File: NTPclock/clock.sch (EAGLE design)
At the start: 28 parts, among them IC1 MAX7219CNG

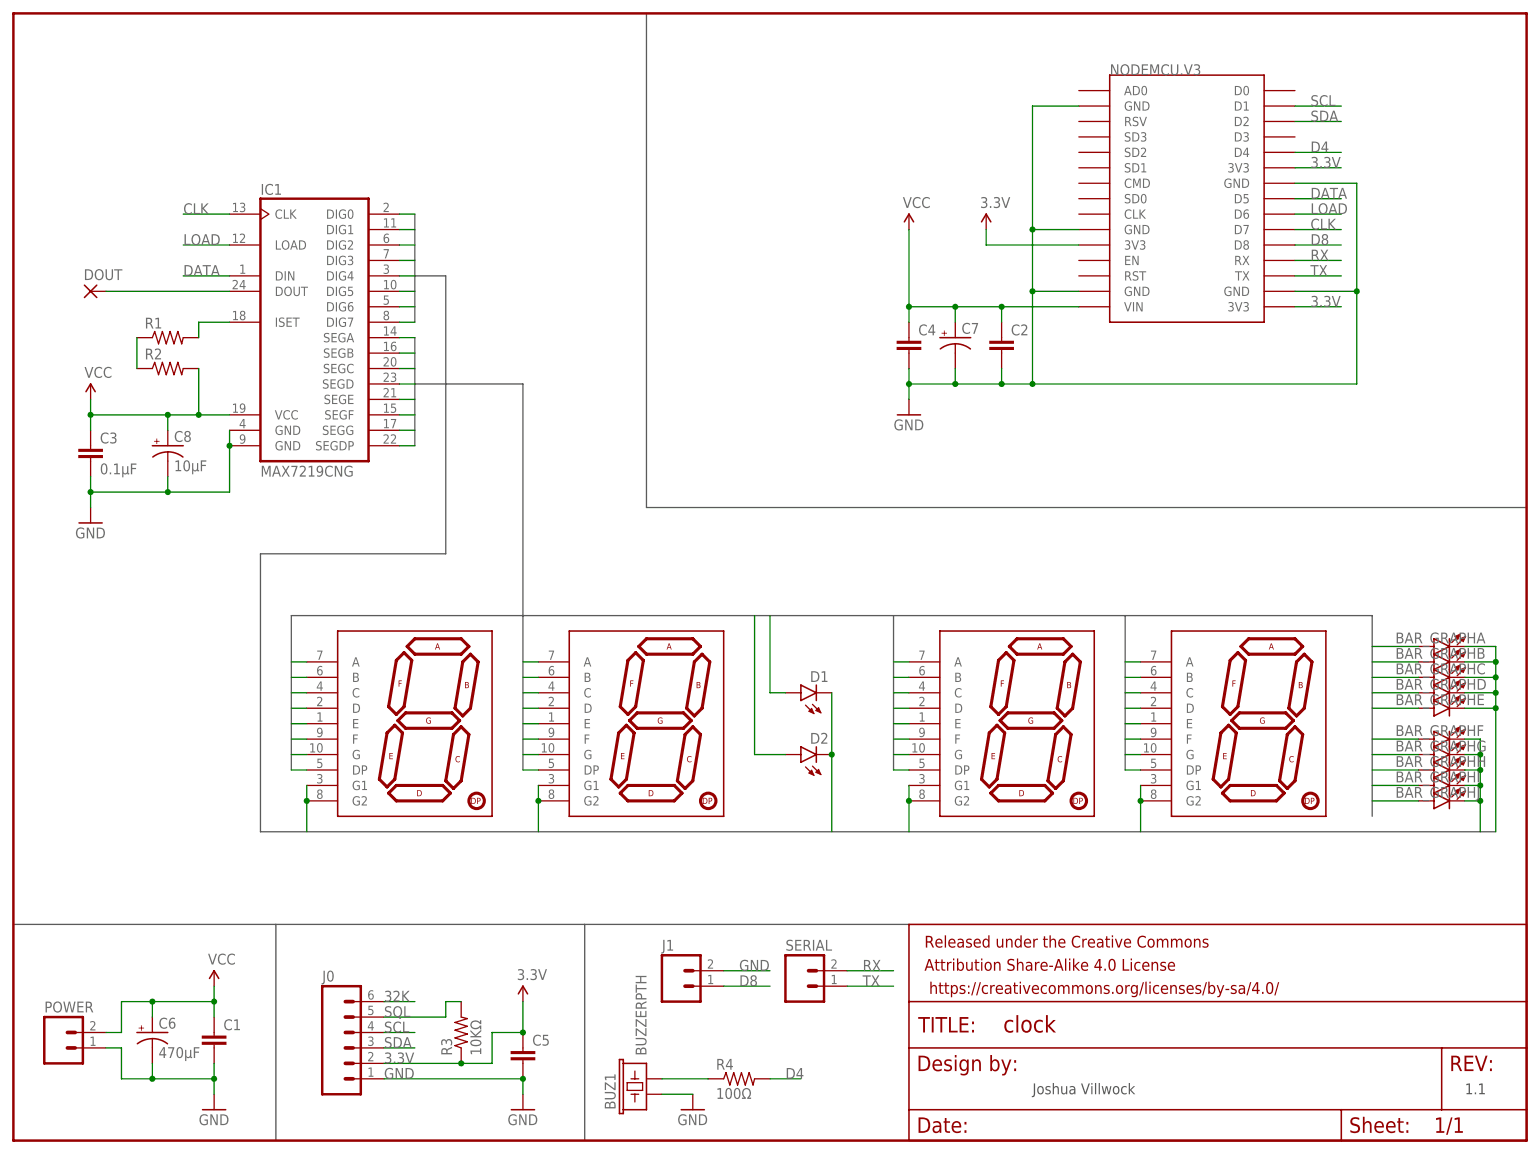
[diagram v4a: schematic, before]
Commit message: Remove Buzzer, add button panel
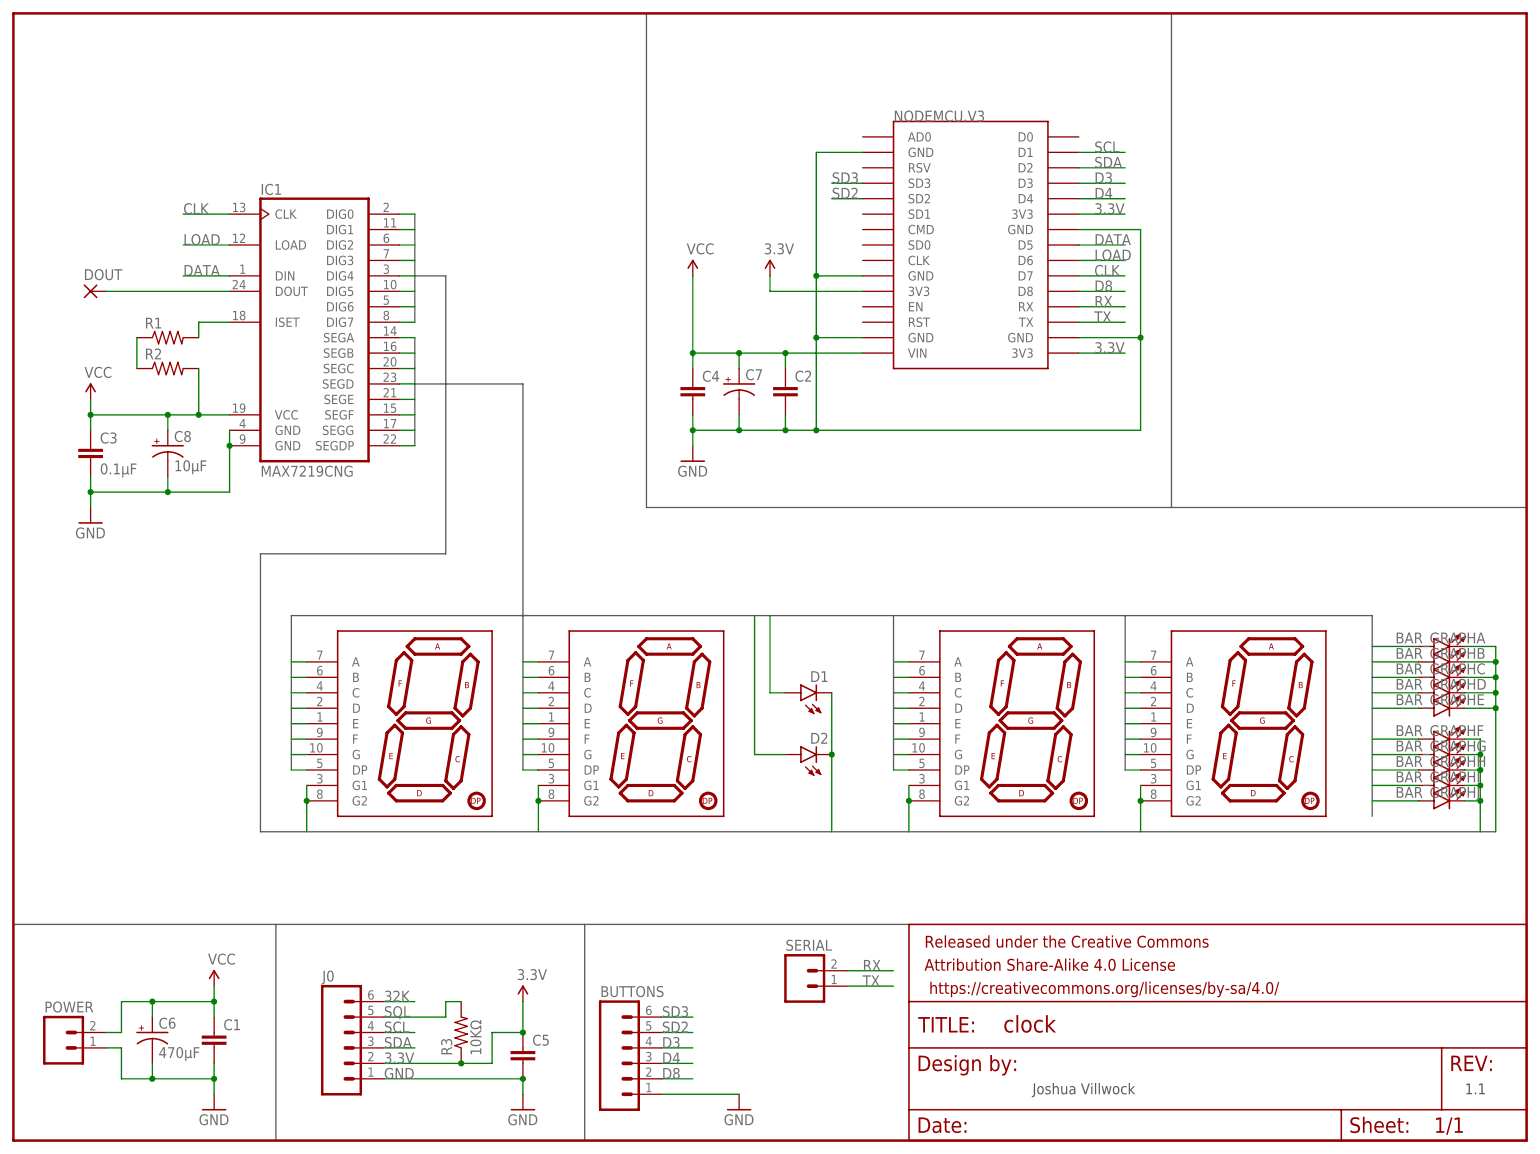
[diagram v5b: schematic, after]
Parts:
- removed BUZ1: BUZZERPTH, SparkFun-Electromechanical:BUZZERPTH
- removed J1: (no value), SparkFun-Connectors:M02PTH
- removed R4: 100Ω, SparkFun-Resistors:RESISTOR1206
- added BUTTONS: (no value), SparkFun-Connectors:M06POLAR
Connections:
- removed net N$8: BUZ1.2, R4.1
- new net D3: BUTTONS.4, NODEMCU.V3.D3
- new net SD2: BUTTONS.5, NODEMCU.V3.SD2
- new net SD3: BUTTONS.6, NODEMCU.V3.SD3
- net D4: now also BUTTONS.3; no longer R4.2
- net D8: now also BUTTONS.2; no longer J1.1
- net GND: now also BUTTONS.1; no longer BUZ1.1, J1.2
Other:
- moved on the sheet: C2, C4, C7, NODEMCU.V3

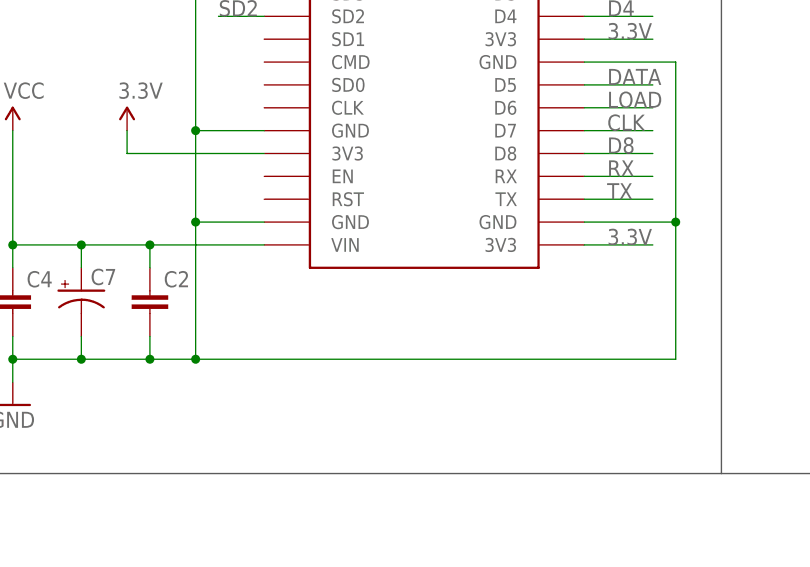
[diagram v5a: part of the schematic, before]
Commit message: Silkscreen changes
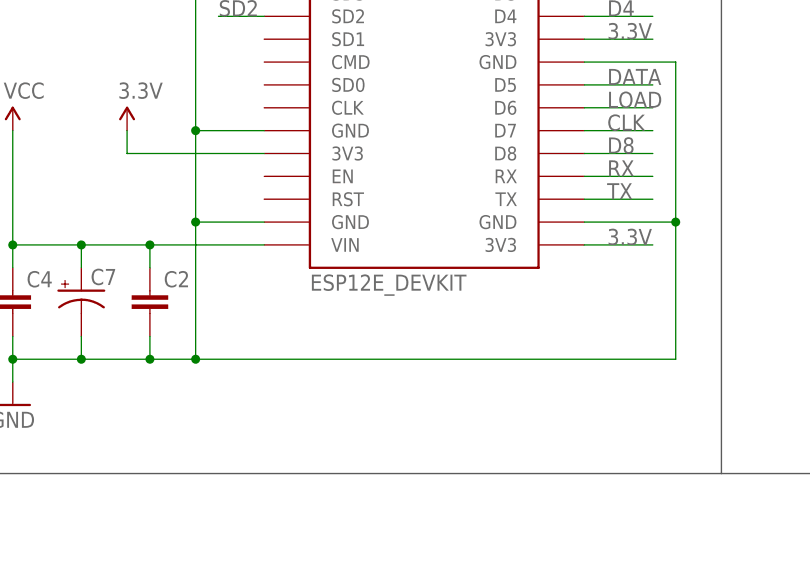
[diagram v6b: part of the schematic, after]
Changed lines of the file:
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@@
 </classes>
 <parts>
-<part name="NODEMCU.V3" library="NODEMCUv1" deviceset="ESP12E_DEVKIT" device="" value=""/>
+<part name="NODEMCU.V3" library="NODEMCUv1" deviceset="ESP12E_DEVKIT" device="" value="ESP12E_DEVKIT"/>
 <part name="IC1" library="max7219" deviceset="MAX7219CNG" device=""/>
 <part name="R1" library="SparkFun-Resistors" deviceset="RESISTOR" device="1206"/>

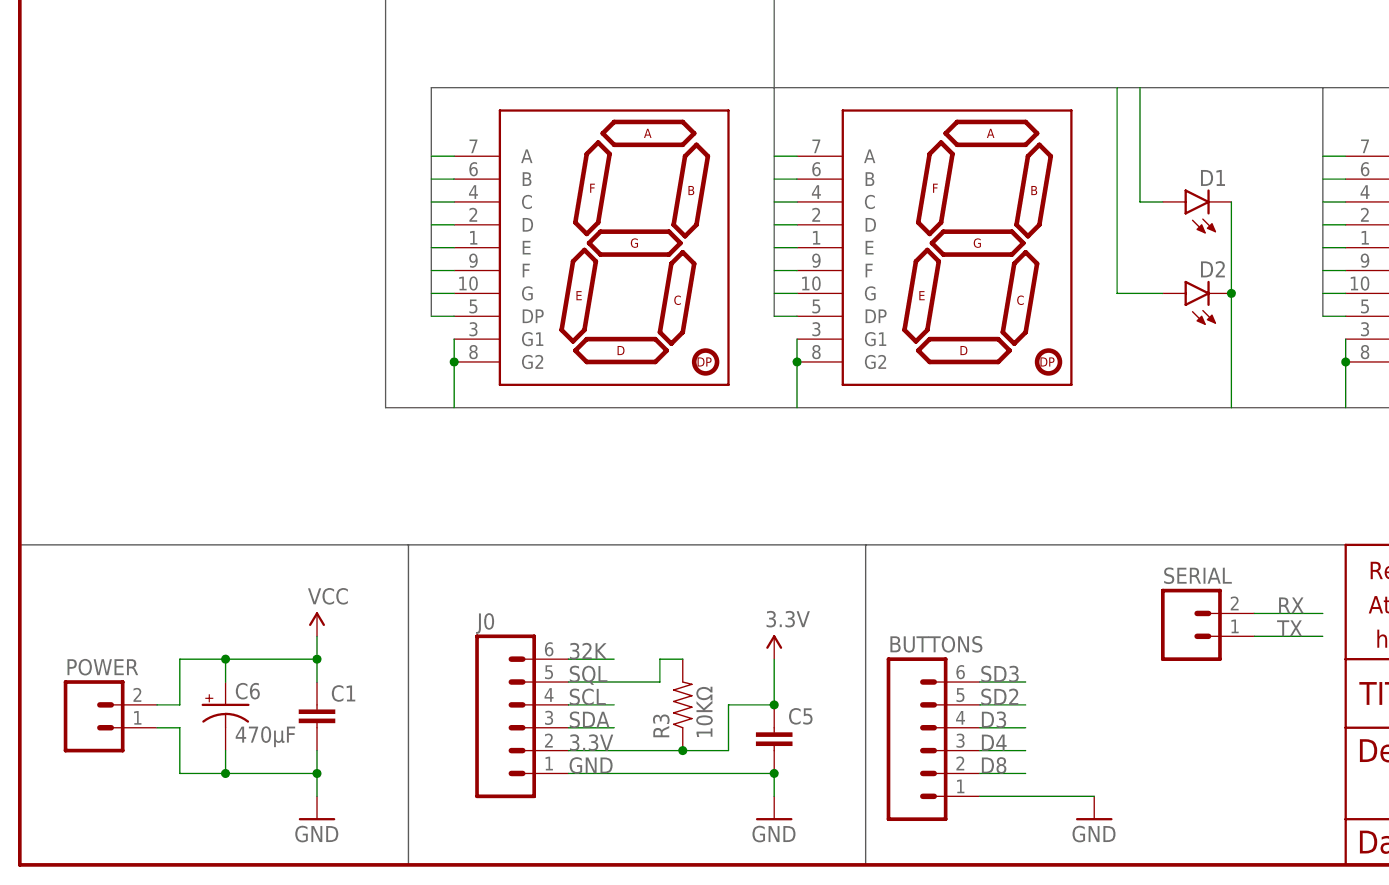
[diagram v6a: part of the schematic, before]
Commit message: Added input protection
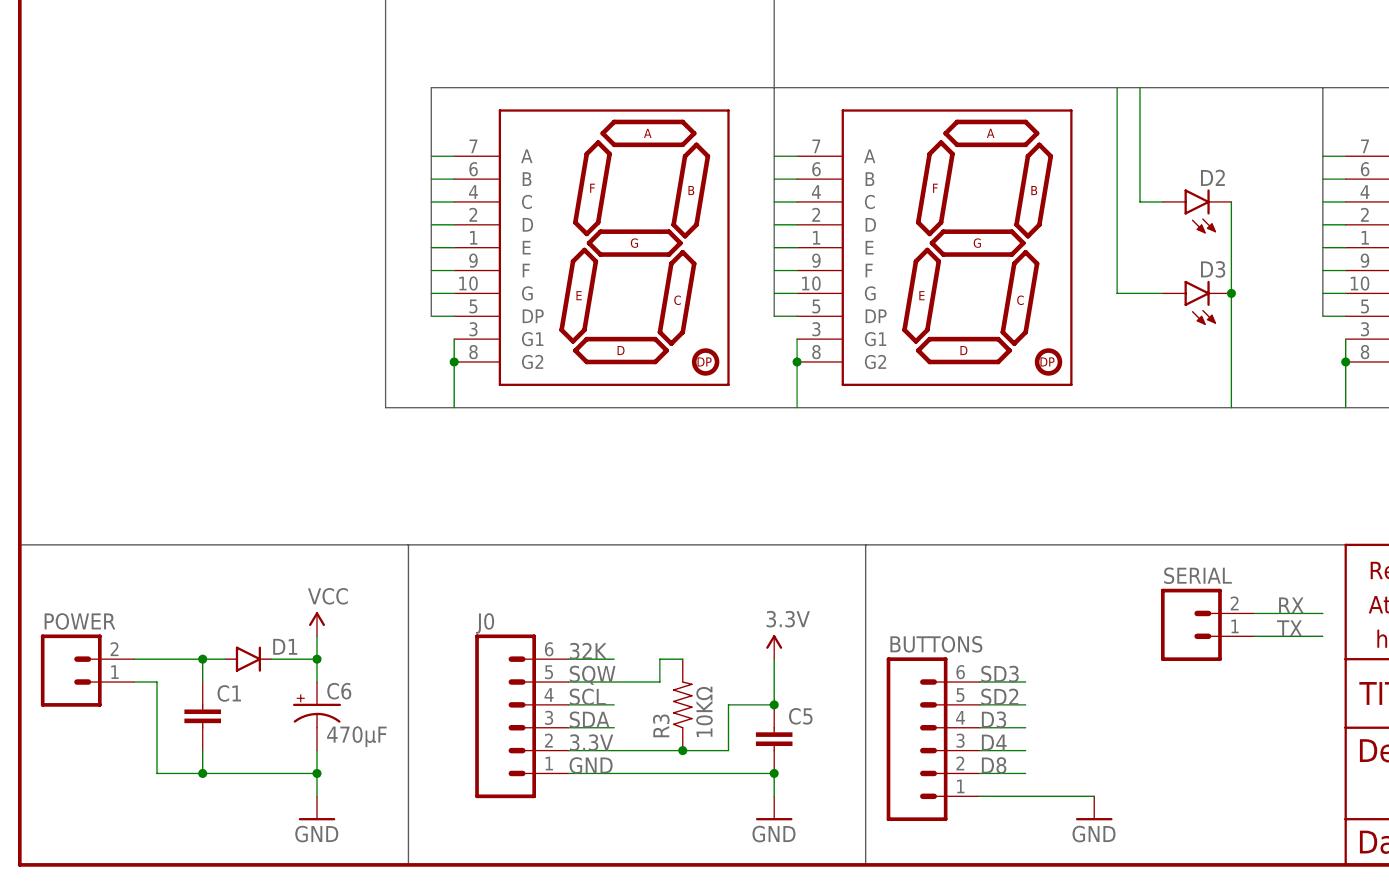
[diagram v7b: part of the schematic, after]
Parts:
- added D3: (no value), SparkFun-LED:LED3MM
- D1: device SparkFun-LED:LED3MM -> SparkFun-DiscreteSemi:DIODE1N4148
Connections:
- net SQL renamed SQW
- new net VIN: C1.1, D1.A, POWER.2
- net D: now also D3.A; no longer D2.A
- net DIGIT4: now also D3.C; no longer D1.C
- net F: now also D2.A; no longer D1.A
- net VCC: now also D1.C; no longer C1.1, POWER.2
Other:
- moved on the sheet: C1, C6, D2, POWER
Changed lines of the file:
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@@
 <part name="GND1" library="SparkFun-Aesthetics" deviceset="GND" device=""/>
 <part name="SUPPLY2" library="SparkFun-Aesthetics" deviceset="3.3V" device=""/>
-<part name="D1" library="SparkFun-LED" deviceset="LED" device="3MM"/>
 <part name="D2" library="SparkFun-LED" deviceset="LED" device="3MM"/>
+<part name="D3" library="SparkFun-LED" deviceset="LED" device="3MM"/>
 <part name="FRAME1" library="SparkFun-Aesthetics" deviceset="FRAME-LETTER" device=""/>
 <part name="SERIAL" library="SparkFun-Connectors" deviceset="M02" device="PTH"/>
 <part name="BUTTONS" library="SparkFun-Connectors" deviceset="M06" device="POLAR"/>
 <part name="GND5" library="SparkFun-Aesthetics" deviceset="GND" device=""/>
+<part name="D1" library="SparkFun-DiscreteSemi" deviceset="DIODE" device="1N4148"/>
 </parts>
 <sheets>
@@
 <instance part="R1" gate="G$1" x="50.8" y="81.28"/>
 <instance part="R2" gate="G$1" x="50.8" y="76.2"/>
-<instance part="C1" gate="G$1" x="58.42" y="-35.56"/>
+<instance part="C1" gate="G$1" x="45.72" y="-35.56"/>
 <instance part="C2" gate="G$1" x="152.4" y="71.12"/>
 <instance part="C3" gate="G$1" x="38.1" y="60.96"/>
 <instance part="C4" gate="G$1" x="137.16" y="71.12"/>
 <instance part="C5" gate="G$1" x="109.22" y="-38.1"/>
-<instance part="C6" gate="G$1" x="48.26" y="-33.02"/>
+<instance part="C6" gate="G$1" x="58.42" y="-33.02"/>
 <instance part="C7" gate="G$1" x="144.78" y="73.66"/>
 <instance part="C8" gate="G$1" x="50.8" y="63.5"/>
-<instance part="POWER" gate="G$1" x="33.02" y="-35.56"/>
+<instance part="POWER" gate="G$1" x="30.48" y="-30.48"/>
 <instance part="J0" gate="G$1" x="81.28" y="-35.56"/>
 <instance part="DIG_3" gate="G$1" x="231.14" y="17.78"/>
@@
 <instance part="GND1" gate="1" x="109.22" y="-45.72"/>
 <instance part="SUPPLY2" gate="G$1" x="149.86" y="91.44"/>
-<instance part="D1" gate="G$1" x="154.94" y="22.86" rot="R90"/>
-<instance part="D2" gate="G$1" x="154.94" y="12.7" rot="R90"/>
+<instance part="D2" gate="G$1" x="154.94" y="22.86" rot="R90"/>
+<instance part="D3" gate="G$1" x="154.94" y="12.7" rot="R90"/>
 <instance part="FRAME1" gate="G$1" x="25.4" y="-50.8"/>
 <instance part="FRAME1" gate="V" x="172.72" y="-50.8"/>
@@
 <instance part="BUTTONS" gate="G$1" x="127" y="-38.1"/>
 <instance part="GND5" gate="1" x="144.78" y="-45.72"/>
+<instance part="D1" gate="G$1" x="50.8" y="-27.94"/>
 </instances>
 <busses>
@@
 </segment>
 <segment>
-<pinref part="POWER" gate="G$1" pin="1"/>
-<wire x1="40.64" y1="-35.56" x2="43.18" y2="-35.56" width="0.1524" layer="91"/>
-<pinref part="C1" gate="G$1" pin="2"/>
 <wire x1="58.42" y1="-43.18" x2="58.42" y2="-40.64" width="0.1524" layer="91"/>
 <pinref part="C6" gate="G$1" pin="-"/>
-<wire x1="58.42" y1="-40.64" x2="58.42" y2="-38.1" width="0.1524" layer="91"/>
-<wire x1="48.26" y1="-38.1" x2="48.26" y2="-40.64" width="0.1524" layer="91"/>
-<junction x="48.26" y="-40.64"/>
+<wire x1="58.42" y1="-38.1" x2="58.42" y2="-40.64" width="0.1524" layer="91"/>
+<junction x="58.42" y="-40.64"/>
 <pinref part="GND2" gate="1" pin="GND"/>
-<wire x1="48.26" y1="-40.64" x2="43.18" y2="-40.64" width="0.1524" layer="91"/>
-<wire x1="43.18" y1="-40.64" x2="43.18" y2="-35.56" width="0.1524" layer="91"/>
-<wire x1="48.26" y1="-40.64" x2="58.42" y2="-40.64" width="0.1524" layer="91"/>
-<junction x="58.42" y="-40.64"/>
+<wire x1="58.42" y1="-40.64" x2="45.72" y2="-40.64" width="0.1524" layer="91"/>
+<pinref part="POWER" gate="G$1" pin="1"/>
+<wire x1="45.72" y1="-40.64" x2="40.64" y2="-40.64" width="0.1524" layer="91"/>
+<wire x1="38.1" y1="-30.48" x2="40.64" y2="-30.48" width="0.1524" layer="91"/>
+<wire x1="40.64" y1="-30.48" x2="40.64" y2="-40.64" width="0.1524" layer="91"/>
+<pinref part="C1" gate="G$1" pin="2"/>
+<wire x1="45.72" y1="-38.1" x2="45.72" y2="-40.64" width="0.1524" layer="91"/>
+<junction x="45.72" y="-40.64"/>
 </segment>
 <segment>
@@
 </segment>
 </net>
-<net name="SQL" class="0">
+<net name="SQW" class="0">
 <segment>
 <pinref part="J0" gate="G$1" pin="5"/>
@@
 </segment>
 <segment>
-<pinref part="D2" gate="G$1" pin="A"/>
+<pinref part="D3" gate="G$1" pin="A"/>
 <wire x1="147.32" y1="12.7" x2="152.4" y2="12.7" width="0.1524" layer="91"/>
 <wire x1="147.32" y1="35.56" x2="147.32" y2="12.7" width="0.1524" layer="91"/>
@@
 </segment>
 <segment>
-<pinref part="D1" gate="G$1" pin="A"/>
+<pinref part="D2" gate="G$1" pin="A"/>
 <wire x1="149.86" y1="22.86" x2="152.4" y2="22.86" width="0.1524" layer="91"/>
 <wire x1="149.86" y1="35.56" x2="149.86" y2="22.86" width="0.1524" layer="91"/>
@@
 </segment>
 <segment>
+<pinref part="D3" gate="G$1" pin="C"/>
+<wire x1="160.02" y1="0" x2="160.02" y2="12.7" width="0.1524" layer="91"/>
 <pinref part="D2" gate="G$1" pin="C"/>
-<wire x1="160.02" y1="0" x2="160.02" y2="12.7" width="0.1524" layer="91"/>
-<pinref part="D1" gate="G$1" pin="C"/>
 <wire x1="160.02" y1="12.7" x2="160.02" y2="22.86" width="0.1524" layer="91"/>
 <junction x="160.02" y="12.7"/>
@@
 <net name="VCC" class="0">
 <segment>
-<pinref part="POWER" gate="G$1" pin="2"/>
-<wire x1="40.64" y1="-33.02" x2="43.18" y2="-33.02" width="0.1524" layer="91"/>
-<wire x1="43.18" y1="-33.02" x2="43.18" y2="-27.94" width="0.1524" layer="91"/>
-<wire x1="43.18" y1="-27.94" x2="48.26" y2="-27.94" width="0.1524" layer="91"/>
-<pinref part="C1" gate="G$1" pin="1"/>
 <wire x1="58.42" y1="-25.4" x2="58.42" y2="-27.94" width="0.1524" layer="91"/>
 <pinref part="C6" gate="G$1" pin="+"/>
-<wire x1="58.42" y1="-27.94" x2="58.42" y2="-30.48" width="0.1524" layer="91"/>
-<wire x1="48.26" y1="-30.48" x2="48.26" y2="-27.94" width="0.1524" layer="91"/>
-<junction x="48.26" y="-27.94"/>
+<wire x1="58.42" y1="-30.48" x2="58.42" y2="-27.94" width="0.1524" layer="91"/>
 <pinref part="SUPPLY1" gate="G$1" pin="VCC"/>
-<wire x1="48.26" y1="-27.94" x2="58.42" y2="-27.94" width="0.1524" layer="91"/>
+<pinref part="D1" gate="G$1" pin="C"/>
+<wire x1="53.34" y1="-27.94" x2="58.42" y2="-27.94" width="0.1524" layer="91"/>
 <junction x="58.42" y="-27.94"/>
 </segment>
@@
 </segment>
 </net>
+<net name="VIN" class="0">
+<segment>
+<pinref part="POWER" gate="G$1" pin="2"/>
+<wire x1="38.1" y1="-27.94" x2="45.72" y2="-27.94" width="0.1524" layer="91"/>
+<pinref part="D1" gate="G$1" pin="A"/>
+<pinref part="C1" gate="G$1" pin="1"/>
+<wire x1="45.72" y1="-27.94" x2="48.26" y2="-27.94" width="0.1524" layer="91"/>
+<wire x1="45.72" y1="-30.48" x2="45.72" y2="-27.94" width="0.1524" layer="91"/>
+<junction x="45.72" y="-27.94"/>
+</segment>
+</net>
